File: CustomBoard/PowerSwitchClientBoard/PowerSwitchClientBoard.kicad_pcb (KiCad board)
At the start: 2 copper layers, 22 parts, among them J1 Conn_01x02, J2 Conn_01x02, J3 Conn_01x02, J4 Conn_01x02, J5 Conn_01x02, J6 Conn_01x02, J7 Conn_01x02, K1 G5LE-1, K2 G5LE-1, Q1 Q_NPN_EBC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

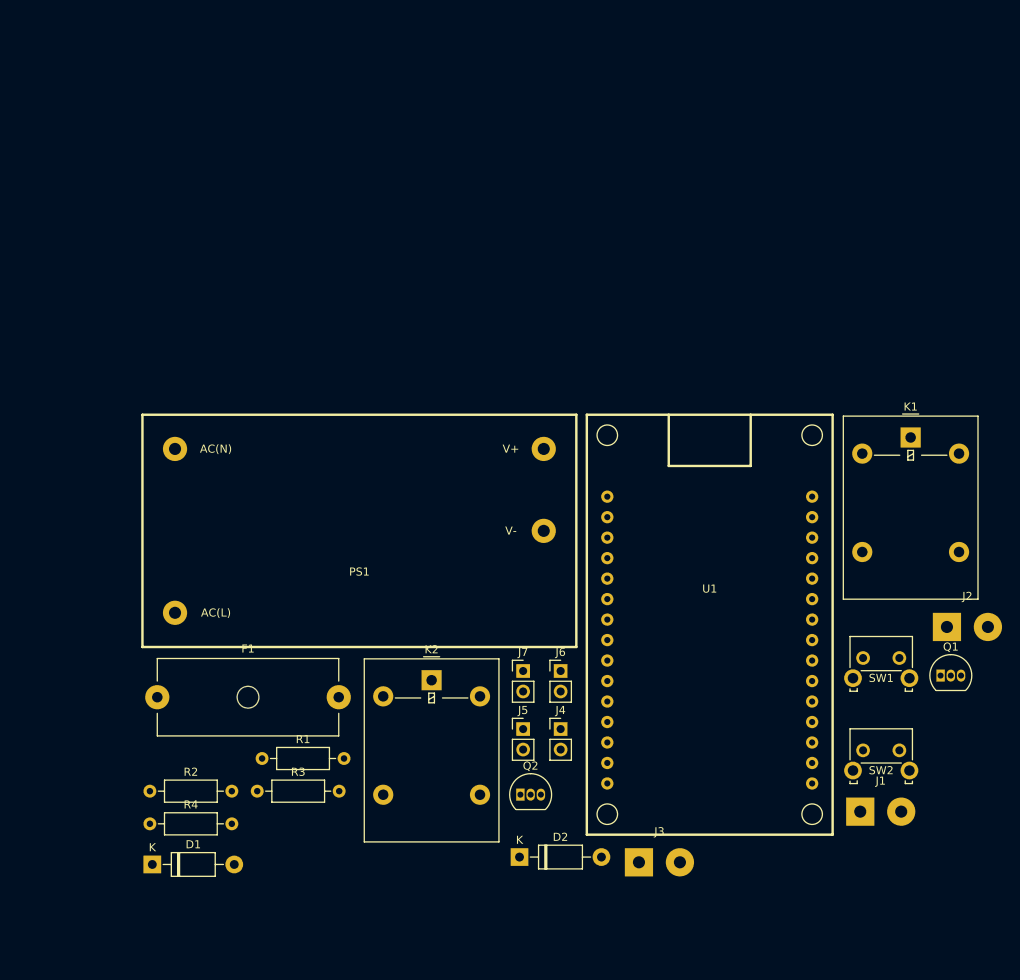
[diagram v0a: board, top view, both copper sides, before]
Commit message: WIP, got docker node/mqtt server working, can't get esphome devices to connect to it through mqtt.
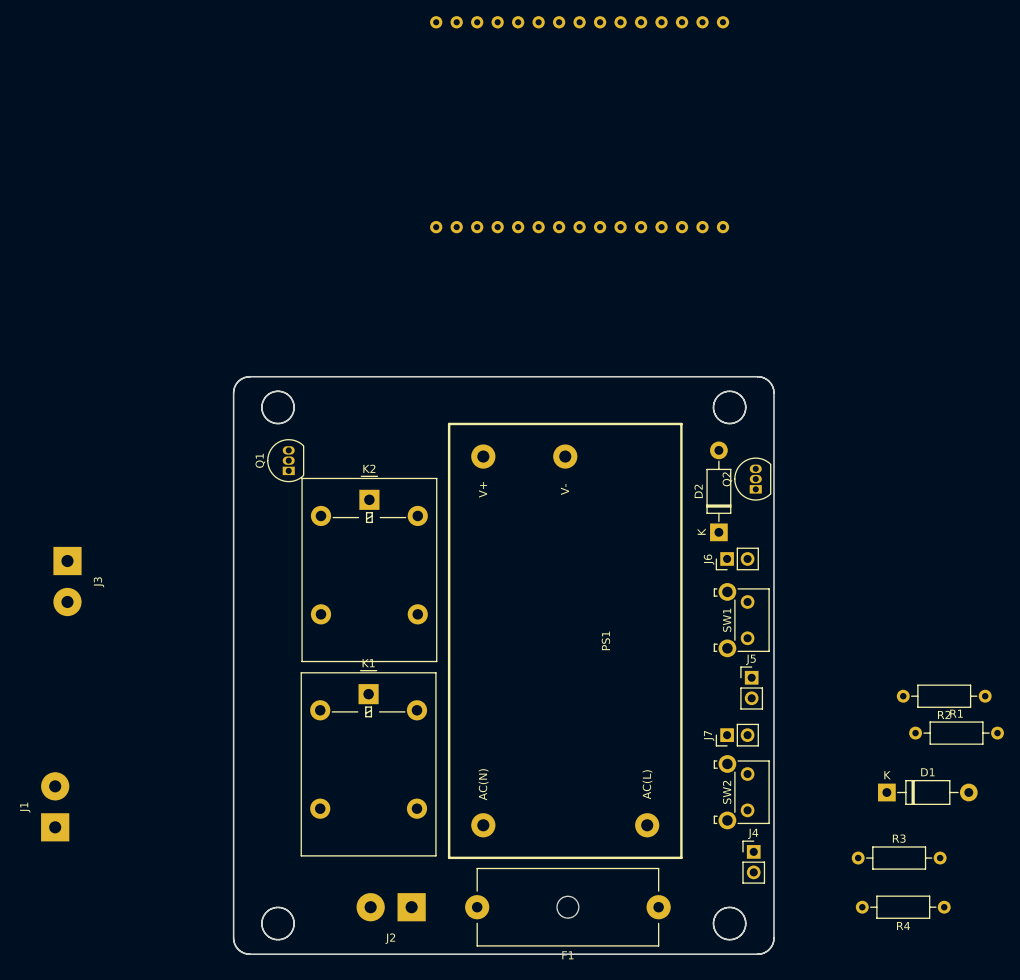
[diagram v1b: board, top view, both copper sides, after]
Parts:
- U1: moved to B.Cu
- moved R2 104.2 mm to (209.6, 110.0), turned to 180 degrees
- moved J1 99.8 mm to (94.2, 126.2), turned to 90 degrees
- moved R4 99.0 mm to (204.5, 136.1), turned to 180 degrees
- moved D1 91.5 mm to (197.4, 121.9)
- moved Q1 84.7 mm to (123.2, 82.0), turned to 90 degrees
- moved R1 81.1 mm to (200.9, 114.6)
- moved J3 80.1 mm to (95.8, 93.2), turned to 270 degrees
- moved R3 75.0 mm to (193.8, 130.0)
- moved J2 74.9 mm to (138.4, 136.1), turned to 180 degrees
- moved K1 74.4 mm to (133.1, 109.7)
- moved F1 67.4 mm to (169.1, 136.1), turned to 180 degrees
- moved Q2 47.8 mm to (181.1, 84.3), turned to 90 degrees
- moved D2 47.2 mm to (176.5, 89.7), turned to 90 degrees
- moved U1 36.4 mm to (177.0, 51.8), turned to 90 degrees
- moved J5 29.0 mm to (180.6, 107.7)
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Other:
- board outline added: 67 x 71.6 mm
